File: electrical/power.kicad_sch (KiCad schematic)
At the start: 56 parts

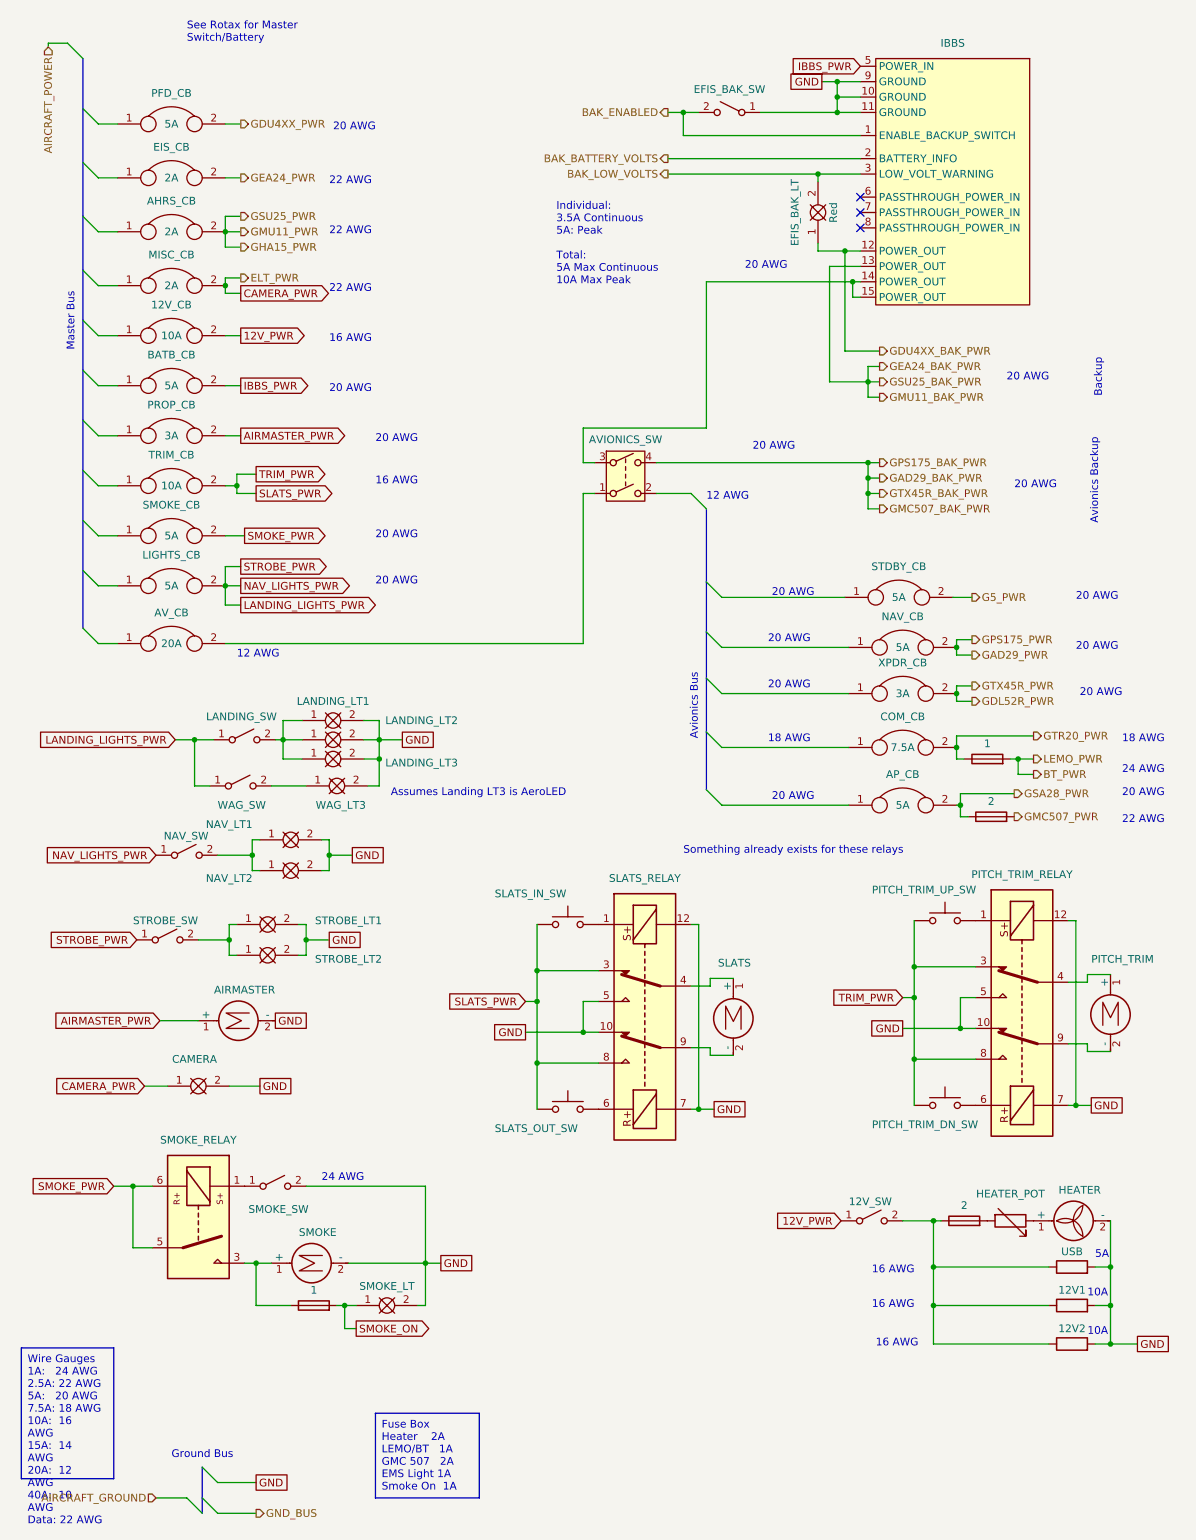
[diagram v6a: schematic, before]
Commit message: Cleaned up power and smoke.
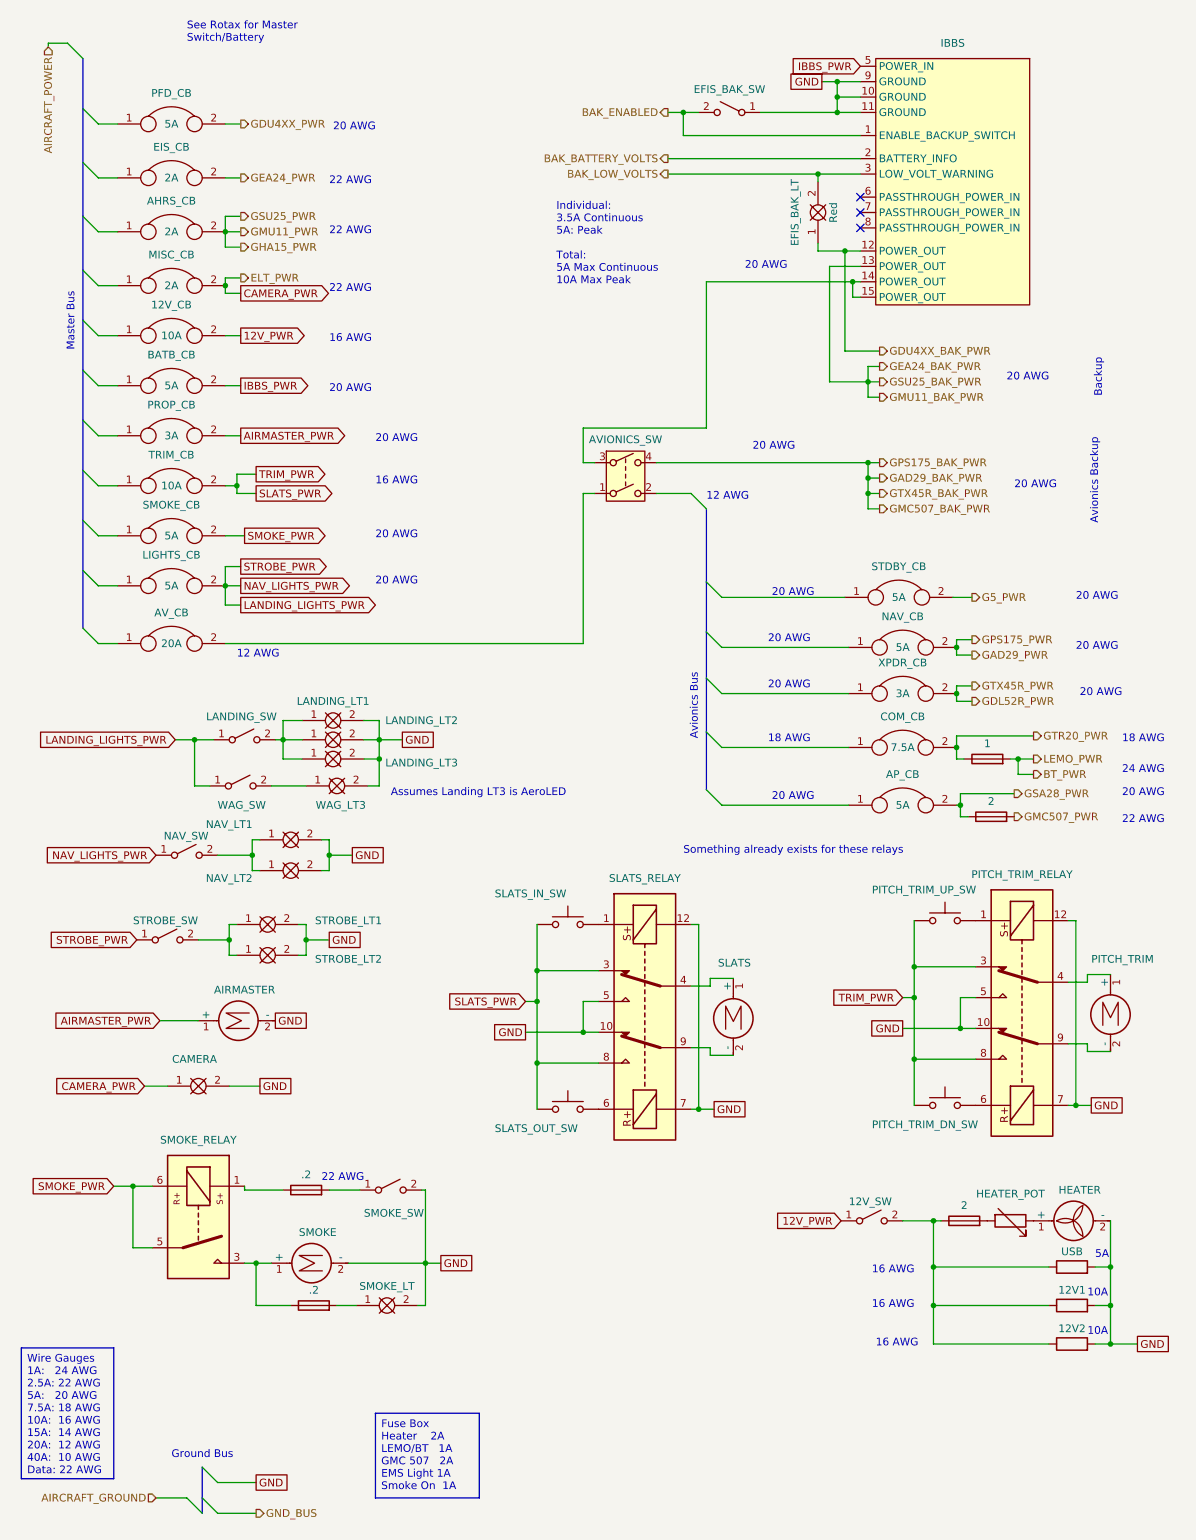
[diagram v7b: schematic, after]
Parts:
- added SMOKE_SW_FS: .2, symbol Device:Fuse
- SMOKE_LT_FS1: value 1 -> .2
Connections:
- net at SMOKE_SW.1 (A): now also SMOKE_SW_FS.2; no longer SMOKE_RELAY.1
- net SMOKE_ON: no longer names the net of SMOKE_LT.1, SMOKE_LT_FS1.2
- new net: SMOKE_RELAY.1, SMOKE_SW_FS.1
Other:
- moved on the sheet: SMOKE_SW
